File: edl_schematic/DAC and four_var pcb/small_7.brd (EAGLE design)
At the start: 160 x 137.3 mm, 45 parts, among them IC1 TL084D, IC2 TL084D, IC3 TL084D

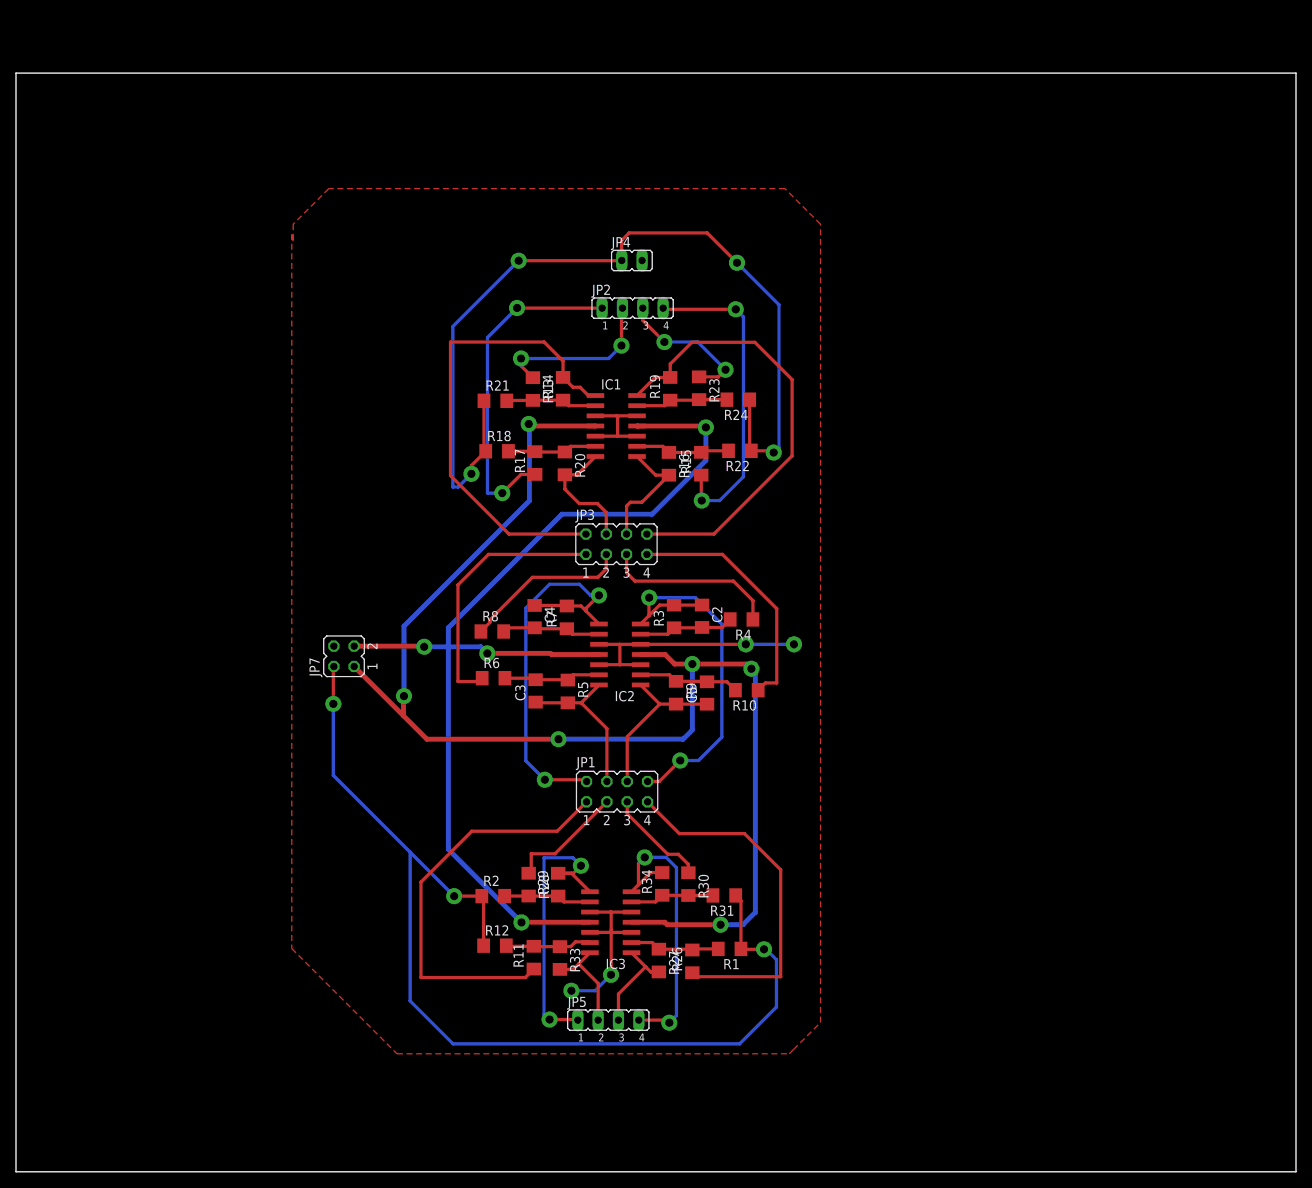
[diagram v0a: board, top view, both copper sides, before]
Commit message: 3v3 power circuit added
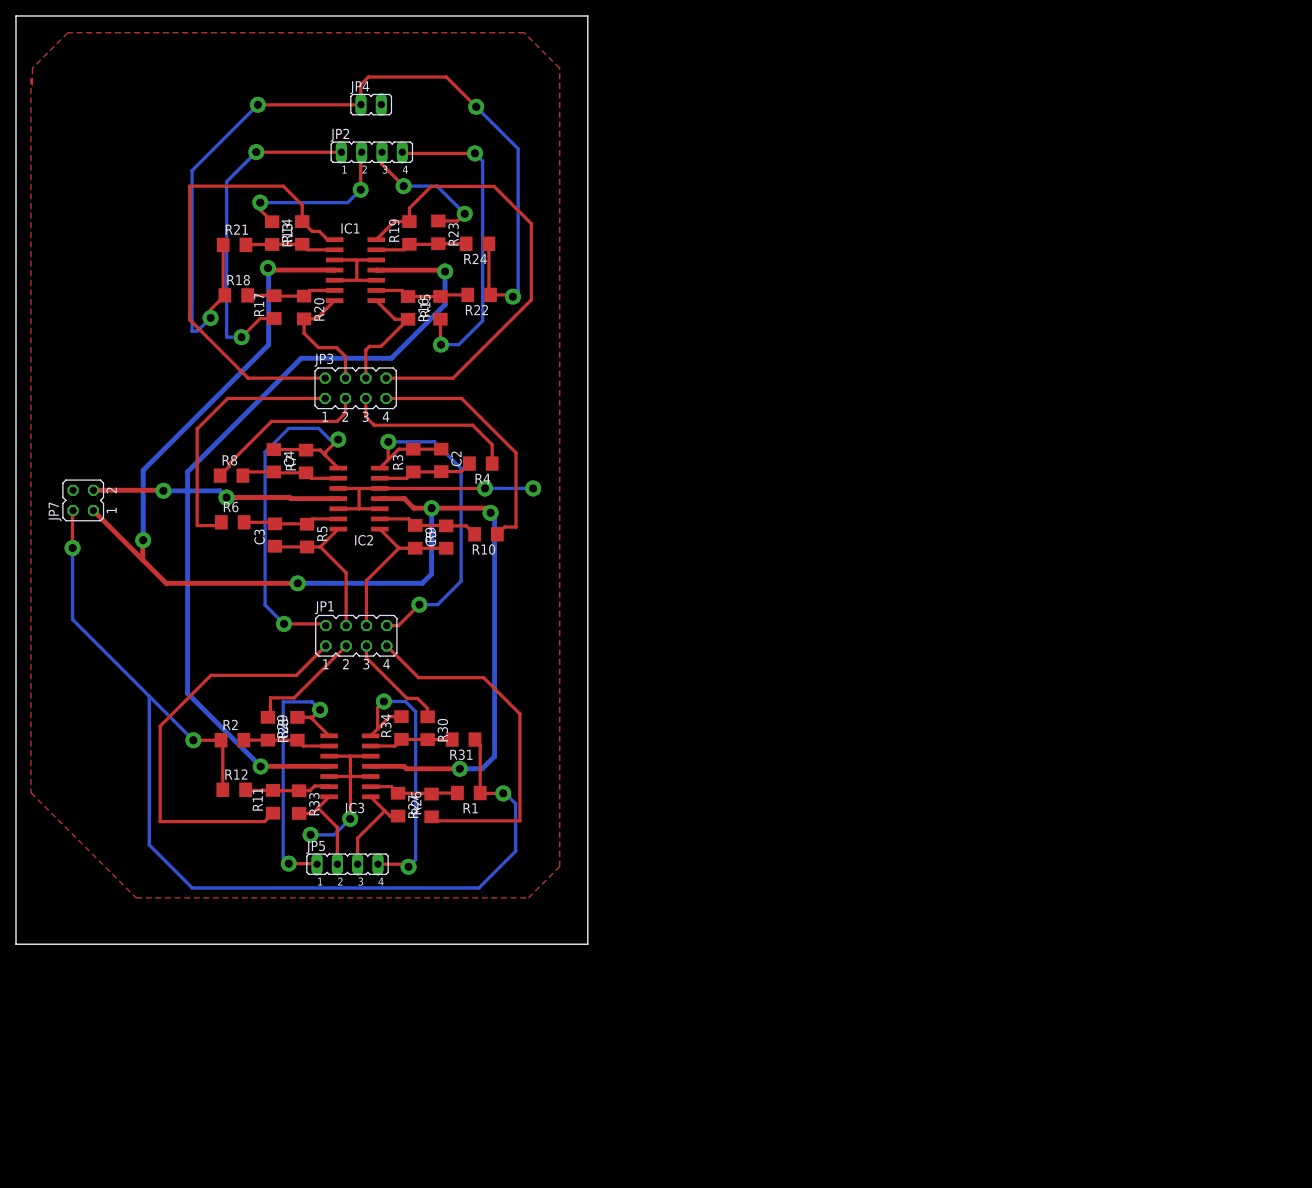
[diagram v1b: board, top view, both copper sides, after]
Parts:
- moved C5 38.0 mm to (53.8, 50.9)
- moved R14 38.0 mm to (35.8, 88.9)
- moved R17 38.0 mm to (32.3, 79.6)
- moved R20 38.0 mm to (36.0, 79.6)
- moved R22 38.0 mm to (57.9, 81.2)
- moved R26 38.0 mm to (51.9, 17.3)
- moved R5 38.0 mm to (36.4, 51.1)
- moved C3 38.0 mm to (32.4, 51.1)
- moved IC1 38.0 mm to (42.4, 84.3)
- moved IC2 38.0 mm to (42.9, 55.7)
- moved JP2 38.0 mm to (44.5, 99.0)
- moved JP3 38.0 mm to (42.5, 69.5)
- moved JP4 38.0 mm to (44.4, 105.0)
- moved JP7 38.0 mm to (8.40, 55.5)
- moved R1 38.0 mm to (56.6, 18.9)
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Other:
- board size 160 x 137.3 mm -> 71.5 x 116 mm
